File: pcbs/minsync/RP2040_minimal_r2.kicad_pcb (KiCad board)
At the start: 2 copper layers, 42 x 42 mm, 39 parts, among them J1 Comm, J2 Comm, J3 Comm, J4 Comm, J5 SWD_CONN, J6 Conn_01x01_Pin, J7 SSD1306, SW1 SW_Push, U1 NCP1117-3.3_SOT223, U2 W25Q128JVS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

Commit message: Get minsync PCB ready for order
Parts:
- removed J1, J2, J3, J4: Comm, RP2040_minimal:pitopi_and_power
- added C2: 100n, Capacitor_SMD:C_0402_1005Metric, F.Cu at (93.3, 105.0)
- added PTP1: Comm, RP2040_minimal:pitopi_and_power, F.Cu at (100.0, 82.5)
- added PTP2: Comm, RP2040_minimal:pitopi_and_power, F.Cu at (82.5, 100.0)
- added PTP3: Comm, RP2040_minimal:pitopi_and_power, F.Cu at (100.0, 117.5)
- added PTP4: Comm, RP2040_minimal:pitopi_and_power, F.Cu at (117.5, 100.2)
- added TP2: TestPoint, Connector_PinHeader_2.54mm:PinHeader_1x01_P2.54mm_Vertical, F.Cu at (98.7, 111.6)
- moved C10 0.20 mm to (102.7, 94.9)
- moved C8 0.20 mm to (101.7, 94.9)
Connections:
- U4 pad 1: +3V3 -> Net-(U4-VDD)
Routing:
- net +3V3: track 31.0 -> 70.9 mm, vias 1 -> 2
- net /SI_CLK2: track 0.00 -> 4.55 mm
- net /GPIO21: track 22.6 -> 18.2 mm
- net /GPIO19: track 20.3 -> 16.2 mm
- net /GPIO29_ADC3: track 40.3 -> 43.3 mm
- net /GPIO28_ADC2: track 45.9 -> 44.0 mm
- net GND: track 25.4 -> 27.2 mm, vias 21 -> 23
- net Net-(U4-VDD): track 0.00 -> 1.44 mm
- net /GPIO18: track 18.5 -> 17.4 mm
- net +1V1: track 14.4 -> 15.3 mm
- net /GPIO6: track 20.3 -> 19.6 mm
- net /GPIO27_ADC1: track 31.4 -> 30.8 mm
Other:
- rule pad_to_mask_clearance: 0.051 -> 0
- board text added: "GPOUT3"
- board text added: "RUN"
- board text added: "SI_CLK2"

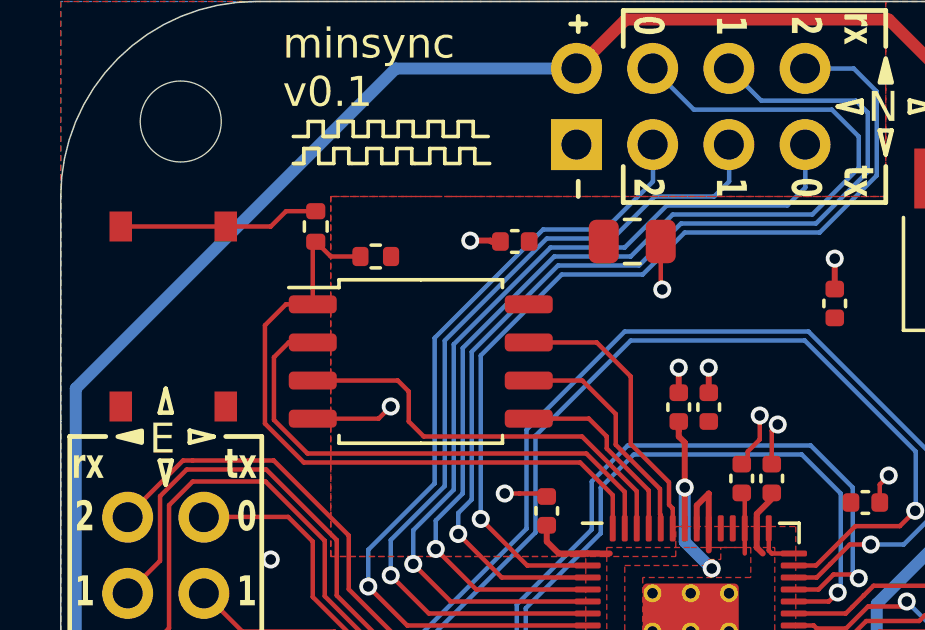
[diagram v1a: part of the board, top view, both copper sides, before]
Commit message: Plot fp text
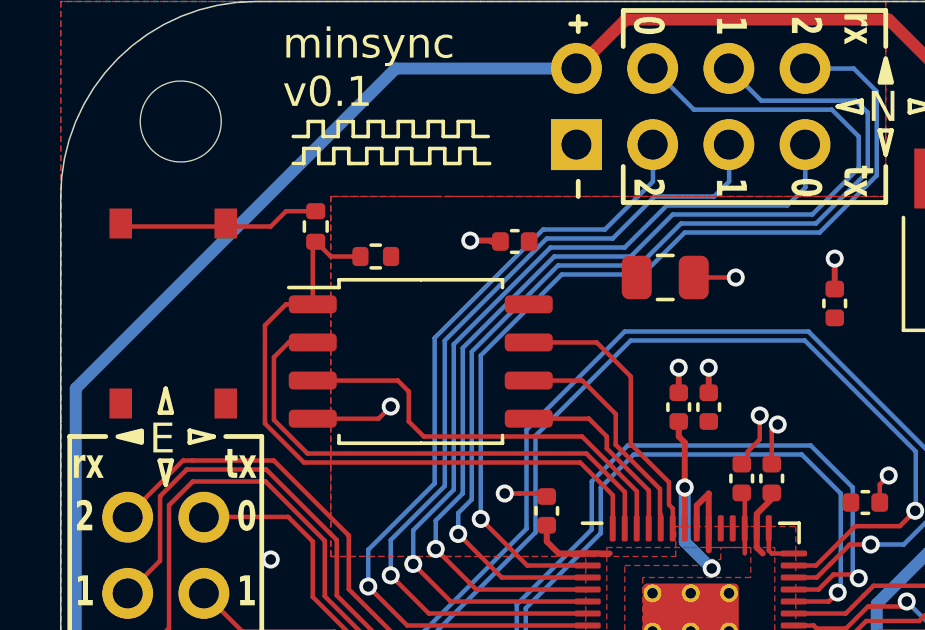
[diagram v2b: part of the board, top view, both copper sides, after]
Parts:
- moved C17 1.63 mm to (99.2, 88.2)
- moved SW1 0.10 mm to (83.0, 89.4)
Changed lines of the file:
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@@
 			(plotreference no)
 			(plotvalue no)
-			(plotfptext no)
+			(plotfptext yes)
 			(plotinvisibletext no)
 			(sketchpadsonfab no)
@@
 	(footprint "Capacitor_SMD:C_0805_2012Metric"
 		(layer "F.Cu")
-		(at 98.05 87)
+		(at 99.15 88.2)
 		(descr "Capacitor SMD 0805 (2012 Metric), square (rectangular) end terminal, IPC_7351 nominal, (Body size source: IPC-SM-782 page 76, https://www.pcb-3d.com/wordpress/wp-content/uploads/ipc-sm-782a_amendment_1_and_2.pdf, https://docs.google.com/spreadsheets/d/1BsfQQcO9C6DZCsRaXUlFlo91Tg2WpOkGARC1WS5S8t0/edit?usp=sharing), generated with kicad-footprint-generator")
 		(tags "capacitor")
@@
 	(footprint "RP2040_minimal:TS-1187A-PushButton"
 		(layer "F.Cu")
-		(at 83 89.5 90)
+		(at 83 89.4 90)
 		(property "Reference" "SW1"
 			(at 0 -0.5 90)
@@
 	)
 	(segment
+		(start 100.1 88.2)
+		(end 101.5 88.2)
+		(width 0.15)
+		(layer "F.Cu")
+		(net 1)
+	)
+	(segment
 		(start 89.595 92.905)
 		(end 90 92.5)
@@
 	)
 	(segment
-		(start 99 87.2)
-		(end 99 88.55)
-		(width 0.15)
-		(layer "F.Cu")
-		(net 1)
-	)
-	(segment
 		(start 102.7 94.42)
 		(end 102.7 93.3)
@@
 	)
 	(segment
-		(start 99 88.55)
-		(end 99.05 88.6)
-		(width 0.15)
-		(layer "F.Cu")
-		(net 1)
-	)
-	(segment
 		(start 97.9125 107.8)
 		(end 97.100001 107.8)
@@
 	)
 	(via
-		(at 99.05 88.6)
+		(at 101.5 88.2)
 		(size 0.6)
 		(drill 0.35)

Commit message: Pos changes
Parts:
- moved JP1 1.20 mm to (107.0, 105.2)
- moved JP2 1.20 mm to (107.0, 105.2)
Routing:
- net /GPIO20: track 4.42 -> 7.75 mm
- net /SI_CLK1: track 9.43 -> 10.8 mm
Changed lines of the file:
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@@
 			(svgprecision 4)
 			(plotframeref no)
-			(viasonmask no)
+			(viasonmask yes)
 			(mode 1)
 			(useauxorigin no)
@@
 	(footprint "Jumper:SolderJumper-2_P1.3mm_Open_RoundedPad1.0x1.5mm"
 		(layer "F.Cu")
-		(at 105.8 105.15 90)
+		(at 107 105.15 90)
 		(descr "SMD Solder Jumper, 1x1.5mm, rounded Pads, 0.3mm gap, open")
 		(tags "solder jumper open")
@@
 	(footprint "Jumper:SolderJumper-2_P1.3mm_Bridged_RoundedPad1.0x1.5mm"
 		(layer "B.Cu")
-		(at 105.8 105.15 90)
+		(at 107 105.15 90)
 		(descr "SMD Solder Jumper, 1x1.5mm, rounded Pads, 0.3mm gap, bridged with 1 copper strip")
 		(tags "net tie solder jumper bridged")
@@
 	)
 	(segment
-		(start 102.7 93.3)
-		(end 102.9 93.1)
+		(start 102.7 94.42)
+		(end 102.7 93.525)
 		(width 0.15)
 		(layer "F.Cu")
@@
 	)
 	(segment
+		(start 103.075 93.15)
+		(end 103.075 93.125)
+		(width 0.15)
+		(layer "F.Cu")
+		(net 1)
+	)
+	(segment
 		(start 101.9 94)
 		(end 102.3 93.6)
@@
 	)
 	(segment
-		(start 102.7 94.42)
-		(end 102.7 93.3)
+		(start 102.7 93.525)
+		(end 103.075 93.15)
 		(width 0.15)
 		(layer "F.Cu")
@@
 	)
 	(via
-		(at 86 97.6)
+		(at 86.7 98)
 		(size 0.6)
 		(drill 0.35)
@@
 	)
 	(via
-		(at 102.9 93.1)
+		(at 103.075 93.125)
 		(size 0.6)
 		(drill 0.35)
@@
 	)
 	(via
-		(at 100.5 113.9)
+		(at 101.5 113)
 		(size 0.6)
 		(drill 0.35)
@@
 	)
 	(segment
-		(start 105.383731 99.183731)
-		(end 105.767462 98.8)
-		(width 0.15)
-		(layer "F.Cu")
-		(net 28)
-	)
-	(segment
-		(start 113.9 95.5)
-		(end 114 95.5)
+		(start 106.092463 98.475)
+		(end 105.767463 98.8)
 		(width 0.15)
 		(layer "F.Cu")
@@
 	)
 	(segment
-		(start 105.767462 98.8)
-		(end 105.767463 98.8)
+		(start 105.167463 99.4)
+		(end 103.4375 99.4)
 		(width 0.15)
 		(layer "F.Cu")
@@
 	)
 	(segment
-		(start 105.767463 98.8)
+		(start 110.925 98.475)
 		(end 106.092463 98.475)
 		(width 0.15)
@@
 	)
 	(segment
-		(start 110.925 98.475)
-		(end 113.9 95.5)
+		(start 105.767463 98.8)
+		(end 105.767462 98.8)
 		(width 0.15)
 		(layer "F.Cu")
@@
 	)
 	(segment
-		(start 105.167463 99.4)
-		(end 105.383731 99.183731)
+		(start 112.7 96.7)
+		(end 110.925 98.475)
 		(width 0.15)
 		(layer "F.Cu")
@@
 	)
 	(segment
-		(start 103.4375 99.4)
+		(start 105.383731 99.183731)
 		(end 105.167463 99.4)
 		(width 0.15)
@@
 	)
 	(segment
-		(start 106.092463 98.475)
-		(end 110.925 98.475)
+		(start 105.767462 98.8)
+		(end 105.383731 99.183731)
 		(width 0.15)
 		(layer "F.Cu")
@@
 	)
 	(via
-		(at 114 95.5)
+		(at 112.7 96.7)
 		(size 0.6)
 		(drill 0.35)
@@
 	)
 	(segment
+		(start 119 92)
+		(end 119 90)
+		(width 0.15)
+		(layer "B.Cu")
+		(net 28)
+	)
+	(segment
 		(start 118.5 92.5)
 		(end 119 92)
@@
 	)
 	(segment
-		(start 114 95.5)
-		(end 117 92.5)
+		(start 112.75 96.65)
+		(end 112.85 96.65)
 		(width 0.15)
 		(layer "B.Cu")
@@
 	)
 	(segment
-		(start 119 92)
-		(end 119 90)
+		(start 112.7 96.7)
+		(end 112.75 96.65)
 		(width 0.15)
 		(layer "B.Cu")
@@
 	)
 	(segment
+		(start 112.85 96.65)
+		(end 117 92.5)
+		(width 0.15)
+		(layer "B.Cu")
+		(net 28)
+	)
+	(segment
 		(start 105.175736 99.9)
 		(end 105.909502 99.166234)
@@
 	)
 	(segment
+		(start 106.9 104.4)
+		(end 107 104.5)
+		(width 0.15)
+		(layer "F.Cu")
+		(net 33)
+	)
+	(segment
+		(start 105.2 104.4)
+		(end 106.9 104.4)
+		(width 0.15)
+		(layer "F.Cu")
+		(net 33)
+	)
+	(segment
 		(start 104.4 101.8)
 		(end 103.4375 101.8)
@@
 	)
 	(via
-		(at 105.8 104.4)
+		(at 105.2 104.4)
 		(size 0.6)
 		(drill 0.35)
@@
 	)
 	(segment
-		(start 105.8 104.3)
-		(end 105.2 103.7)
+		(start 107 104.5)
+		(end 105.3 104.5)
 		(width 0.15)
 		(layer "B.Cu")
@@
 	)
 	(segment
-		(start 105.8 104.5)
-		(end 105.8 104.4)
+		(start 105.3 104.5)
+		(end 105.2 104.4)
 		(width 0.15)
 		(layer "B.Cu")
@@
 	)
 	(segment
-		(start 105.2 102.3)
-		(end 105.2 103.7)
-		(width 0.15)
-		(layer "B.Cu")
-		(net 33)
-	)
-	(segment
-		(start 105.8 104.4)
-		(end 105.8 104.3)
+		(start 105.2 104.4)
+		(end 105.2 102.3)
 		(width 0.15)
 		(layer "B.Cu")
@@
 	)
 	(segment
-		(start 104.4 106.6)
-		(end 104.575736 106.6)
+		(start 99.6 108.175001)
+		(end 99.6 108.4)
 		(width 0.15)
 		(layer "F.Cu")
@@
 	(segment
 		(start 104.1 106.9)
-		(end 104.4 106.6)
-		(width 0.15)
-		(layer "F.Cu")
-		(net 54)
-	)
-	(segment
-		(start 99.6 108.175001)
-		(end 99.6 108.4)
+		(end 105.2 105.8)
 		(width 0.15)
 		(layer "F.Cu")
@@
 	)
 	(segment
-		(start 104.575736 106.6)
-		(end 105.587868 105.587868)
+		(start 105.2 105.8)
+		(end 107 105.8)
 		(width 0.15)
 		(layer "F.Cu")
@@
 	)
 	(segment
-		(start 105.8 105.8)
-		(end 105.8 107.4)
+		(start 105.8 107)
+		(end 107 105.8)
+		(width 0.15)
+		(layer "B.Cu")
+		(net 55)
+	)
+	(segment
+		(start 105.8 107.4)
+		(end 105.8 107)
 		(width 0.15)
 		(layer "B.Cu")

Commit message: Order minsync
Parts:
- moved TP2 1.10 mm to (98.7, 112.7), turned to 180 degrees
- turned TP1 to -90 degrees
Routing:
- net /SI_CLK2: track 4.55 -> 5.67 mm

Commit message: Debug minsync PCB
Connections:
- U4 pad 7: unconnected-(U4-VDDO-Pad7) -> Net-(U4-VDD)
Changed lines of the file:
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@@
 	(net 50 "/XB")
 	(net 51 "/XA")
-	(net 52 "unconnected-(U4-VDDO-Pad7)")
-	(net 53 "Net-(D1-A)")
-	(net 54 "/SI_CLK1")
-	(net 55 "Net-(JP2-A)")
-	(net 56 "Net-(U4-VDD)")
+	(net 52 "Net-(D1-A)")
+	(net 53 "/SI_CLK1")
+	(net 54 "Net-(JP2-A)")
+	(net 55 "Net-(U4-VDD)")
 	(footprint "Capacitor_SMD:C_0805_2012Metric"
 		(layer "F.Cu")
@@
 		)
 		(fp_text user "${REFERENCE}"
-			(at 0 0 360)
+			(at 0 0 0)
 			(layer "F.Fab")
 			(effects
@@
 		(tags "Through hole pin header THT 1x01 2.54mm single row")
 		(property "Reference" "TP2"
-			(at 0 -2.33 360)
+			(at 0 -2.33 0)
 			(layer "F.SilkS")
 			(hide yes)
@@
 		)
 		(property "Value" "TestPoint"
-			(at 0 2.33 360)
+			(at 0 2.33 0)
 			(layer "F.Fab")
 			(effects
@@
 			(size 1 0.5)
 			(layers "F.Cu" "F.Mask")
-			(net 54 "/SI_CLK1")
+			(net 53 "/SI_CLK1")
 			(pinfunction "A")
 			(pintype "passive")
@@
 			(layers "F.Cu" "F.Paste" "F.Mask")
 			(roundrect_rratio 0.25)
-			(net 53 "Net-(D1-A)")
+			(net 52 "Net-(D1-A)")
 			(pinfunction "A")
 			(pintype "passive")
@@
 			(layers "F.Cu" "F.Paste" "F.Mask")
 			(roundrect_rratio 0.25)
-			(net 56 "Net-(U4-VDD)")
+			(net 55 "Net-(U4-VDD)")
 			(pintype "passive")
 		)
@@
 			(layers "F.Cu" "F.Paste" "F.Mask")
 			(roundrect_rratio 0.25)
-			(net 53 "Net-(D1-A)")
+			(net 52 "Net-(D1-A)")
 			(pintype "passive")
 		)
@@
 			(layers "F.Cu" "F.Paste" "F.Mask")
 			(roundrect_rratio 0.25)
-			(net 55 "Net-(JP2-A)")
+			(net 54 "Net-(JP2-A)")
 			(pintype "passive")
 		)
@@
 			(layers "F.Cu" "F.Paste" "F.Mask")
 			(roundrect_rratio 0.25)
-			(net 56 "Net-(U4-VDD)")
+			(net 55 "Net-(U4-VDD)")
 			(pinfunction "VDD")
 			(pintype "power_in")
@@
 			(layers "F.Cu" "F.Paste" "F.Mask")
 			(roundrect_rratio 0.25)
-			(net 52 "unconnected-(U4-VDDO-Pad7)")
+			(net 55 "Net-(U4-VDD)")
 			(pinfunction "VDDO")
 			(pintype "power_in")
@@
 			(layers "F.Cu" "F.Paste" "F.Mask")
 			(roundrect_rratio 0.25)
-			(net 54 "/SI_CLK1")
+			(net 53 "/SI_CLK1")
 			(pinfunction "CLK1")
 			(pintype "output")
@@
 			(size 1 0.5)
 			(layers "B.Cu" "B.Mask")
-			(net 55 "Net-(JP2-A)")
+			(net 54 "Net-(JP2-A)")
 			(pinfunction "A")
 			(pintype "passive")
@@
 		(width 0.15)
 		(layer "F.Cu")
-		(net 53)
+		(net 52)
 	)
 	(segment
@@
 		(width 0.15)
 		(layer "F.Cu")
-		(net 53)
+		(net 52)
 	)
 	(segment
@@
 		(width 0.15)
 		(layer "F.Cu")
-		(net 54)
+		(net 53)
 	)
 	(segment
@@
 		(width 0.15)
 		(layer "F.Cu")
-		(net 54)
+		(net 53)
 	)
 	(segment
@@
 		(width 0.15)
 		(layer "F.Cu")
-		(net 54)
+		(net 53)
 	)
 	(segment
@@
 		(width 0.15)
 		(layer "F.Cu")
-		(net 54)
+		(net 53)
 	)
 	(segment
@@
 		(width 0.15)
 		(layer "F.Cu")
-		(net 54)
+		(net 53)
 	)
 	(via
@@
 		(drill 0.35)
 		(layers "F.Cu" "B.Cu")
-		(net 54)
+		(net 53)
 	)
 	(via
@@
 		(drill 0.35)
 		(layers "F.Cu" "B.Cu")
-		(net 54)
+		(net 53)
 	)
 	(segment
@@
 		(width 0.15)
 		(layer "B.Cu")
-		(net 54)
+		(net 53)
 	)
 	(segment
@@
 		(width 0.15)
 		(layer "B.Cu")
-		(net 54)
+		(net 53)
 	)
 	(segment
@@
 		(width 0.15)
 		(layer "B.Cu")
-		(net 54)
+		(net 53)
 	)
 	(segment
@@
 		(width 0.15)
 		(layer "B.Cu")
-		(net 54)
+		(net 53)
 	)
 	(segment
@@
 		(width 0.15)
 		(layer "F.Cu")
-		(net 55)
+		(net 54)
 	)
 	(segment
@@
 		(width 0.15)
 		(layer "F.Cu")
-		(net 55)
+		(net 54)
 	)
 	(via
@@
 		(drill 0.35)
 		(layers "F.Cu" "B.Cu")
-		(net 55)
+		(net 54)
 	)
 	(segment
@@
 		(width 0.15)
 		(layer "B.Cu")
-		(net 55)
+		(net 54)
 	)
 	(segment
@@
 		(width 0.15)
 		(layer "B.Cu")
-		(net 55)
+		(net 54)
 	)
 	(segment
@@
 		(width 0.3)
 		(layer "F.Cu")
-		(net 56)
+		(net 55)
 	)
 	(segment
@@
 		(width 0.3)
 		(layer "F.Cu")
-		(net 56)
+		(net 55)
 	)
 	(zone

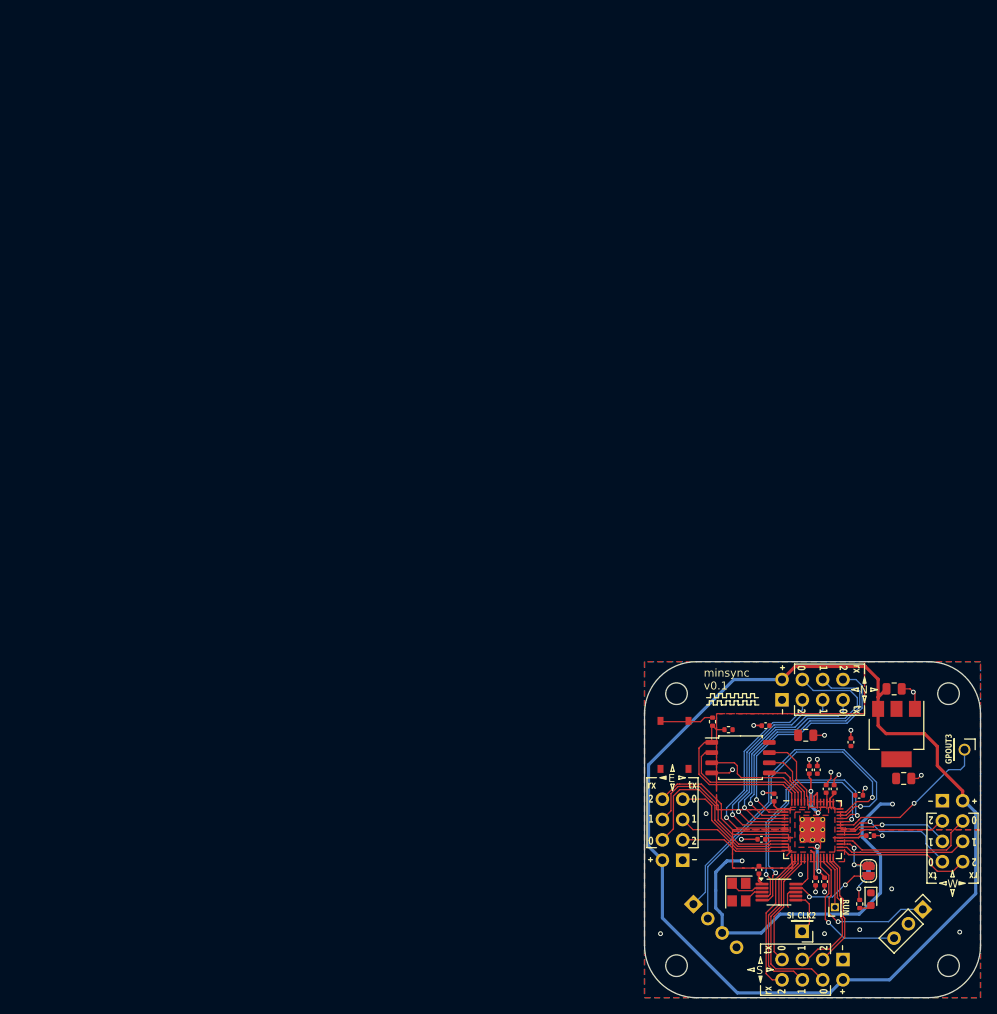
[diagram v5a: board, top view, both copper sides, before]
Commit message: Test more of the hardware / make PCB modifications for v0.2
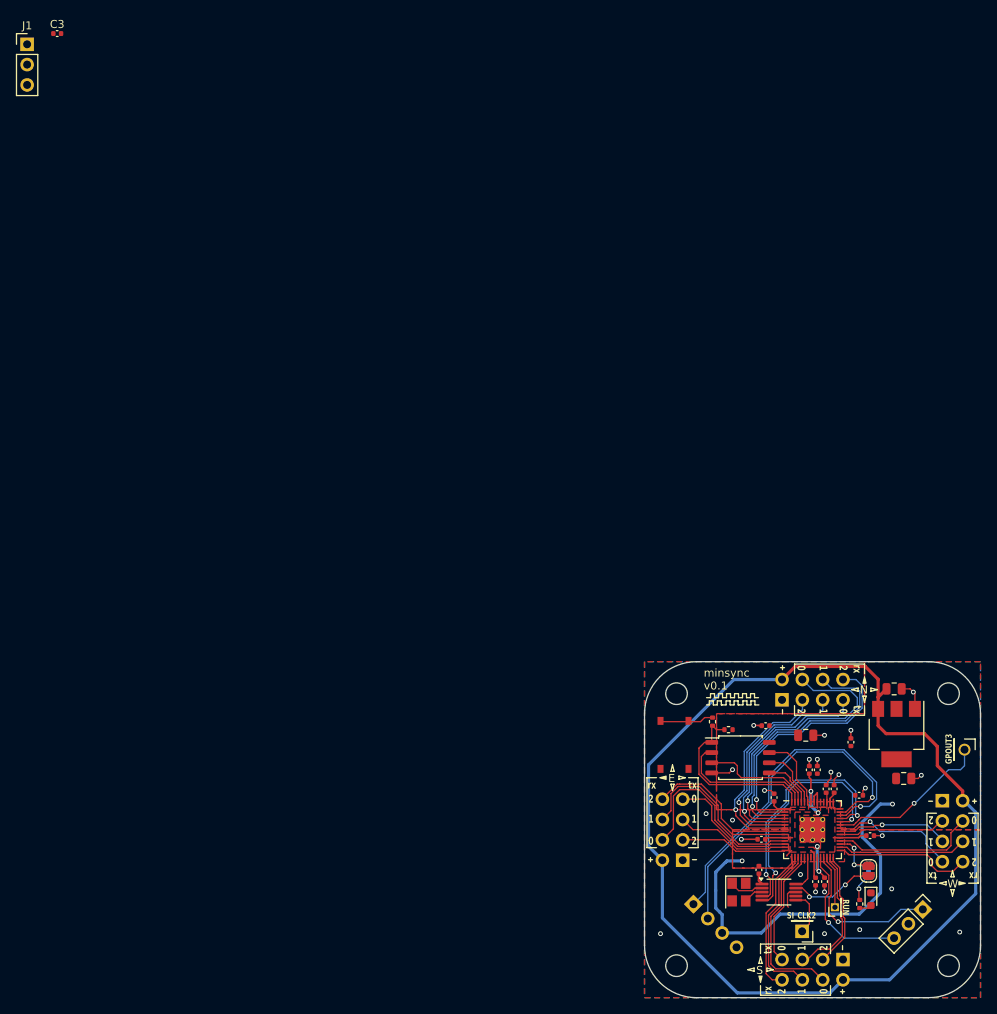
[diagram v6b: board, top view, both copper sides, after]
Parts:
- added C3: 0.47uF, Capacitor_SMD:C_0402_1005Metric, F.Cu at (5.58, 0.48)
- added J1: SWD_JST, Connector_PinHeader_2.54mm:PinHeader_1x03_P2.54mm_Vertical, F.Cu at (1.82, 1.82)
- C2: value 100n -> 0.47uF
- J5: value SWD_CONN -> SWD_HEADERS
- R3: value 470R -> 1k
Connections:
- C2 pad 2: Net-(U4-VDD) -> GND
- U4 pad 1: Net-(U4-VDD) -> +3V3
- U4 pad 7: Net-(U4-VDD) -> +3V3
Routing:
- net /GPIO5: track 27.7 -> 26.0 mm
- net Net-(U4-VDD): track 1.44 -> 0.00 mm
- net (no net): track 0.00 -> 1.44 mm
- net /GPIO4: track 28.6 -> 27.4 mm
- net /GPIO3: track 29.5 -> 28.8 mm
- net /GPIO0: track 30.8 -> 31.5 mm
- net GND: track 27.3 -> 27.1 mm, vias 23 -> 24
